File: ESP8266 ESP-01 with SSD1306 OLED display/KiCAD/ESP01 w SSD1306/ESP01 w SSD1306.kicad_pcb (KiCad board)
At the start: 2 copper layers, 30.5 x 47.6 mm, 6 parts, among them U1 AMS1117-3.3, U2 ESP-01h, U3 SSD1306_I2C_display

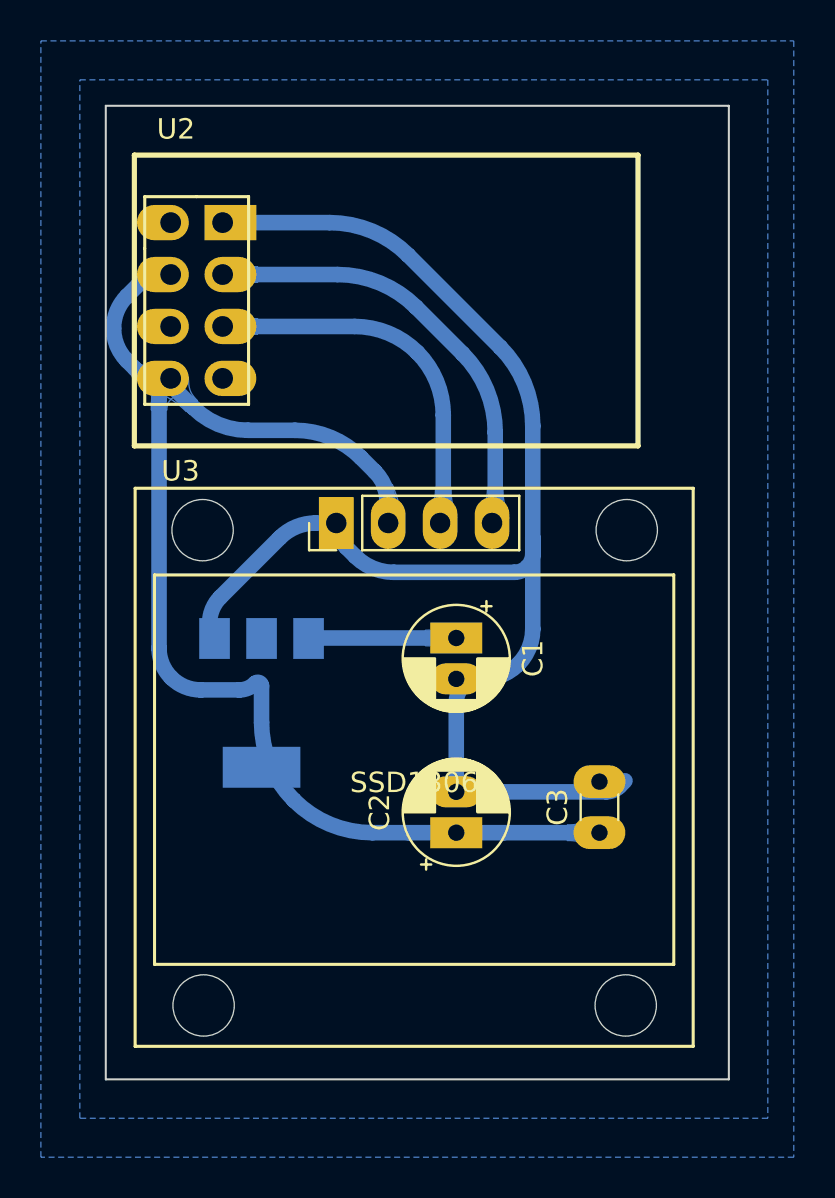
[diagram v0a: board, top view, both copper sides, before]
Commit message: esp w 1306
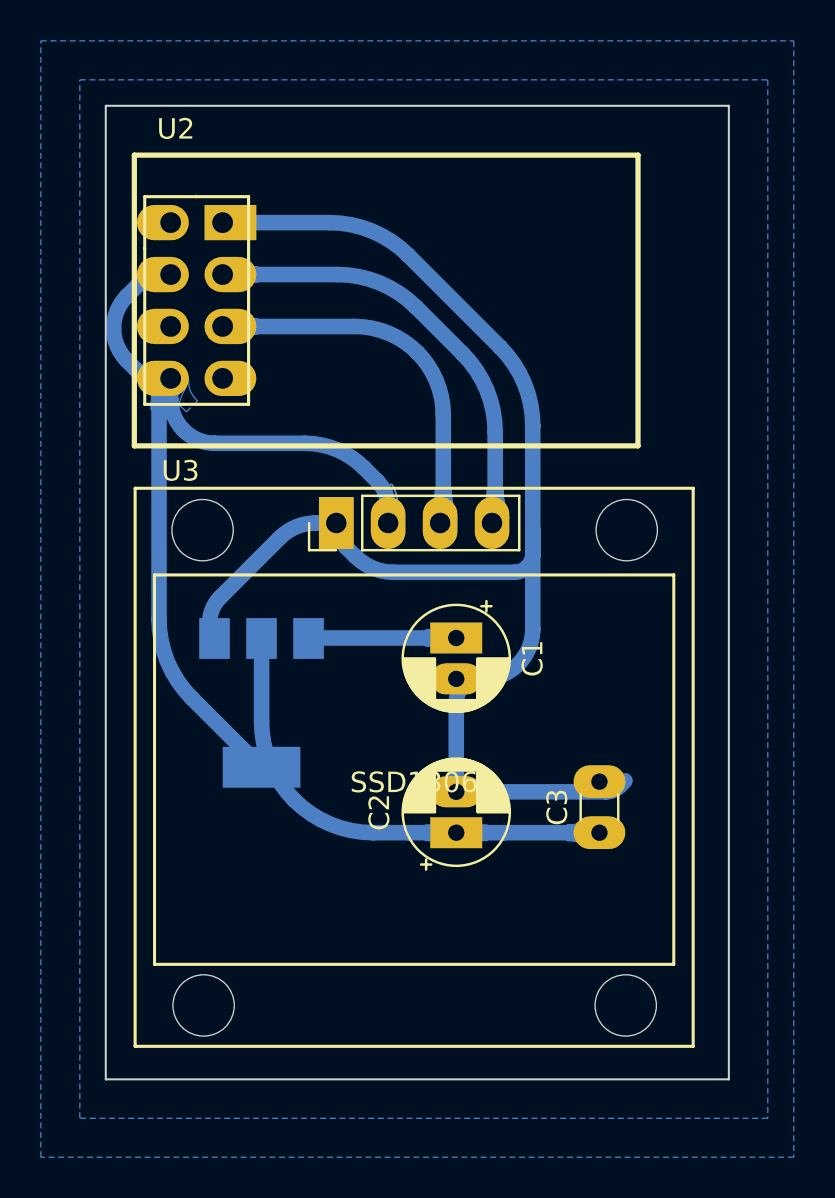
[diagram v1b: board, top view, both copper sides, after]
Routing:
- net +3V3: track 63.9 -> 68.3 mm
